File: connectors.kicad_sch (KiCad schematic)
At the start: 12 parts, among them J1 JST_SH_1x4_SM04B-SRSS-TB-LF-SN, J2 Molex_Nano-Fit_1x2_105313-220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, J3 USB-C_GCT_USB4105-GF-A, J4 JST_SH_1x4_SM04B-SRSS-TB-LF-SN, U1 TPD4E02B04DQA, U2 TPD4E02B04DQA

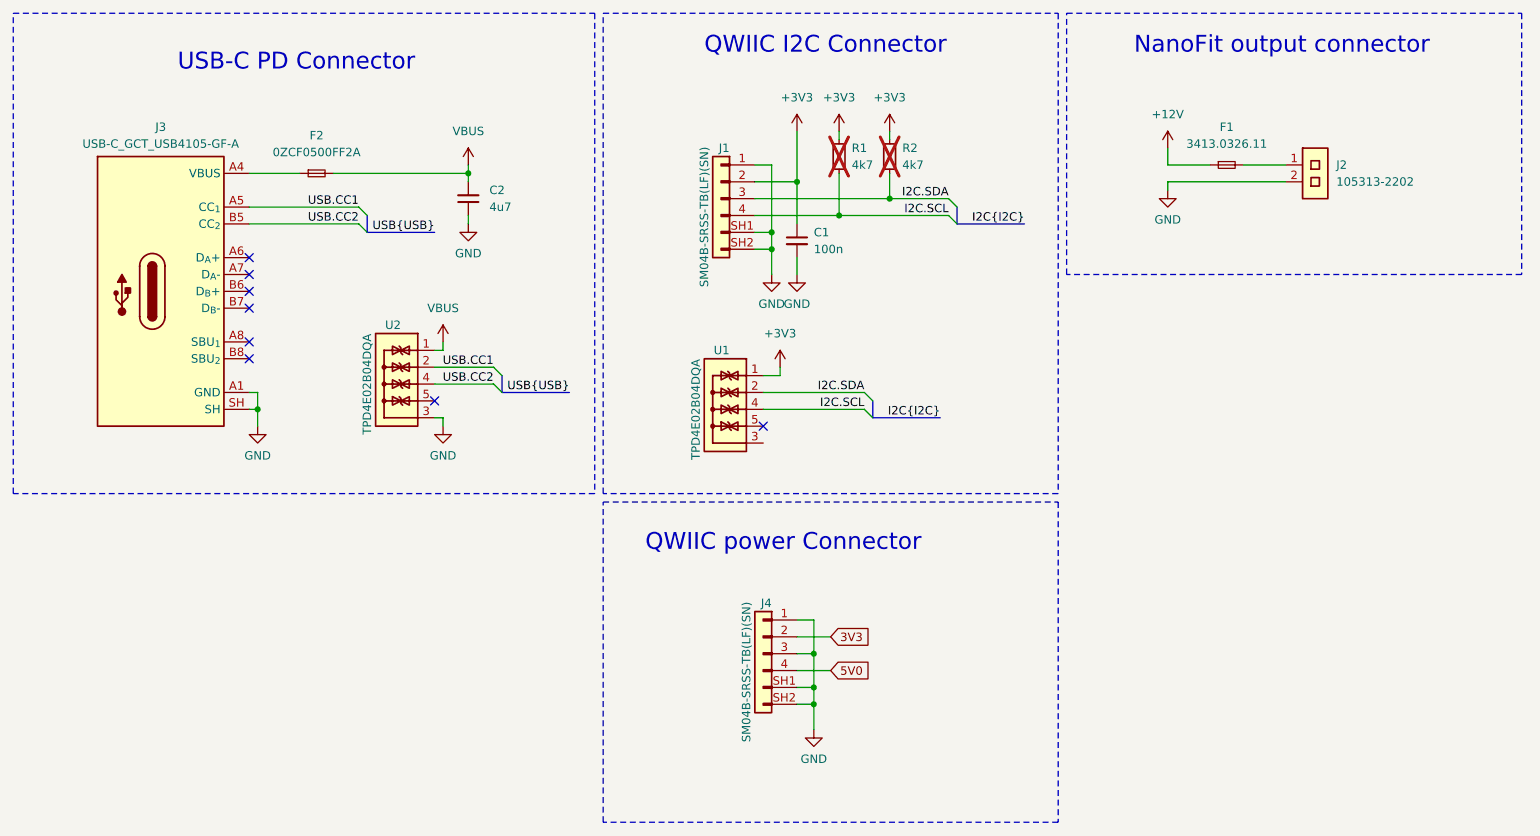
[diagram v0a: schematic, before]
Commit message: [#57006] Change C17, R25, R26
Improve connections
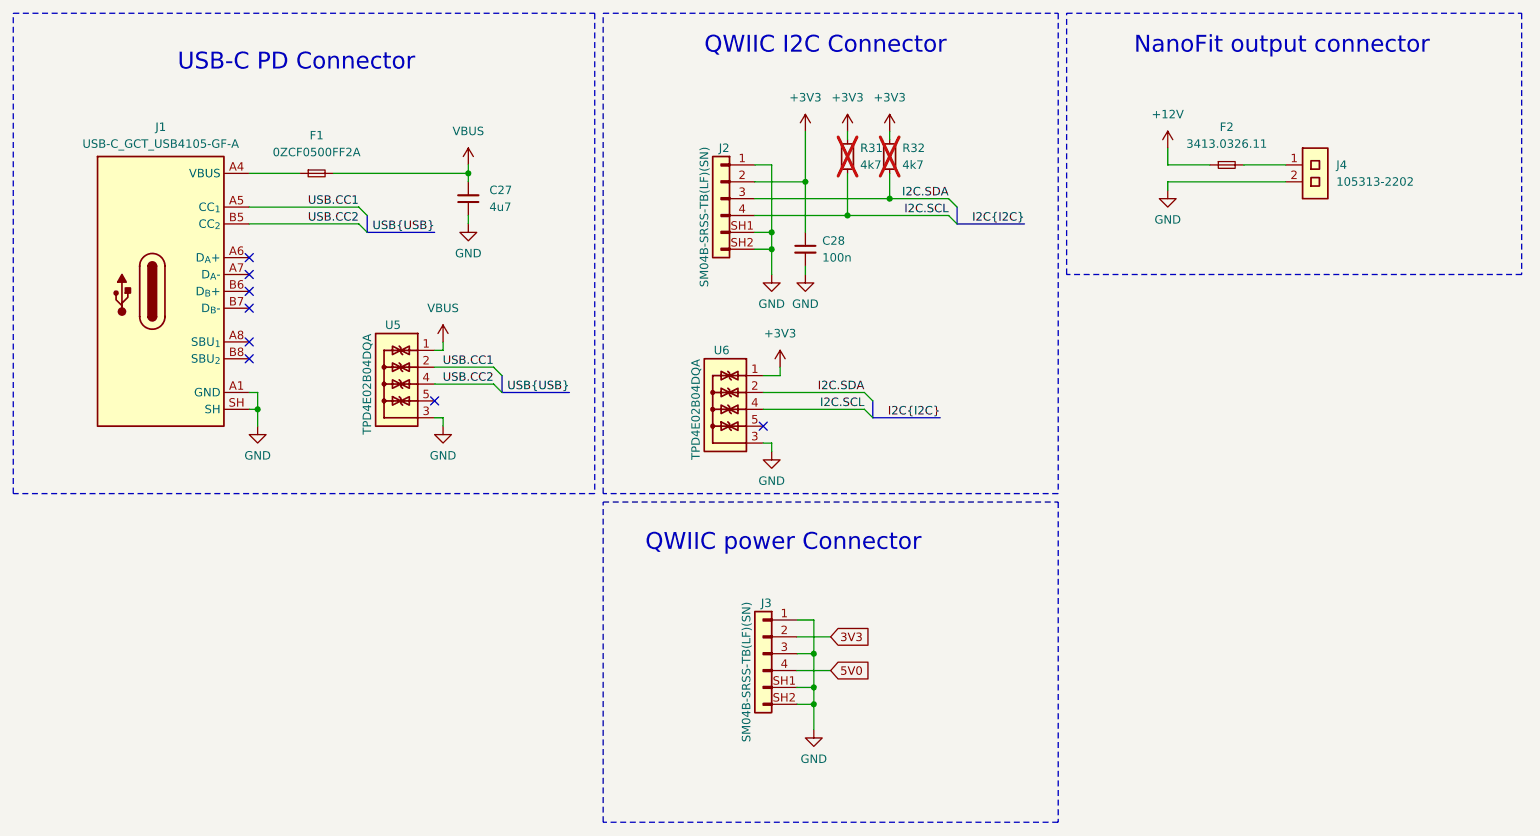
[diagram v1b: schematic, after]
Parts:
- renumbered C2 to C27, C1 to C28, F2 to F1, F1 to F2, J3 to J1, J1 to J2, J4 to J3, J2 to J4, R1 to R31, R2 to R32, U2 to U5, U1 to U6
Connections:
- net GND: now also U6.3, U6.8
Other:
- moved on the sheet: C28, R31

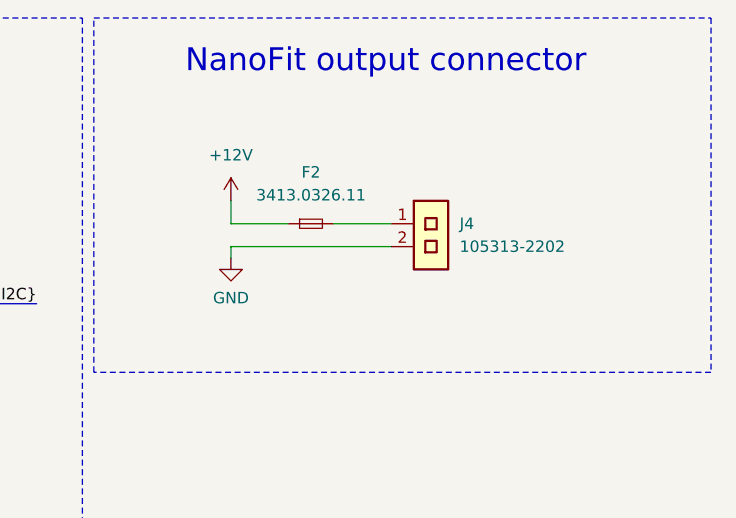
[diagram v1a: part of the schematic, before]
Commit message: [#57006] Add a TVS diode on output
Move power components to a new sheet
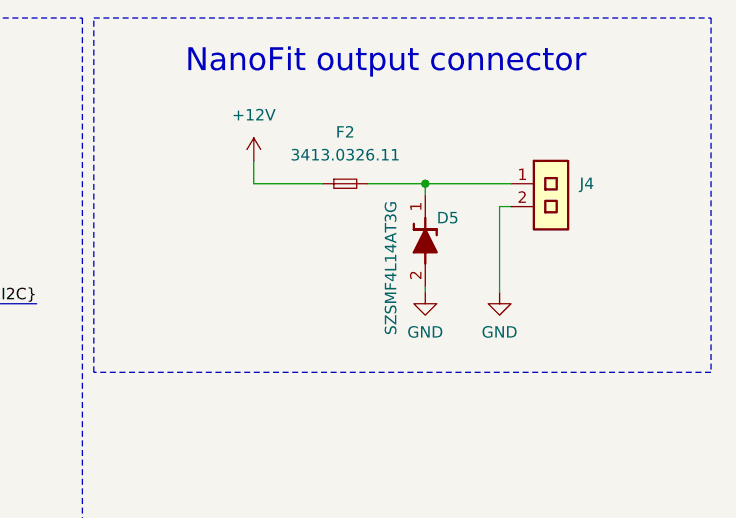
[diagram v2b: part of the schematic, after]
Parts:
- added D5: SZSMF4L14AT3G, antmicro-footprints:SOD-123FL, symbol antmicroTVSDiodes:SZSMF4L14AT3G
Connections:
- net GND: now also D5.2
- net at F2.2, J4.1: now also D5.1
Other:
- moved on the sheet: F2, J4
